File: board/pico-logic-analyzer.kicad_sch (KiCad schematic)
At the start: 25 parts, among them J1 Conn_02x03_Odd_Even, J11 Conn_01x01, SW1 SW_Push, U1 LM2665M6, U2 LM4040DBZ-5

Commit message: added export script
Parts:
- A1: footprint Module_RaspberryPi_Pico:RaspberryPi_Pico_Common_THT -> Module_RaspberryPi_Pico:RaspberryPi_Pico_Common
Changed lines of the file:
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@@
 		(at 128.27 194.31 0)
 		(unit 1)
-		(exclude_from_sim no)
+		(exclude_from_sim yes)
 		(in_bom no)
 		(on_board no)
@@
 			)
 		)
-		(property "Sim.Enable" "0"
-			(at 128.27 194.31 0)
-			(effects
-				(font
-					(size 1.27 1.27)
-				)
-				(hide yes)
-			)
-		)
 		(instances
 			(project "pico-logic-analyzer"
@@
 		(at 110.49 195.58 0)
 		(unit 1)
-		(exclude_from_sim no)
+		(exclude_from_sim yes)
 		(in_bom no)
 		(on_board no)
@@
 		)
 		(property "Description" "Open Hardware logo, small"
-			(at 110.49 195.58 0)
-			(effects
-				(font
-					(size 1.27 1.27)
-				)
-				(hide yes)
-			)
-		)
-		(property "Sim.Enable" "0"
 			(at 110.49 195.58 0)
 			(effects
@@
 			)
 		)
-		(property "Footprint" "Module_RaspberryPi_Pico:RaspberryPi_Pico_Common_THT"
+		(property "Footprint" "Module_RaspberryPi_Pico:RaspberryPi_Pico_Common"
 			(at 148.59 139.7 0)
 			(effects

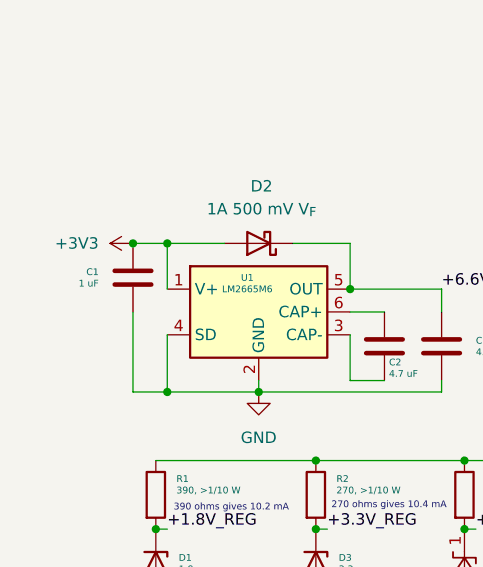
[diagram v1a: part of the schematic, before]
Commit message: 2.0 first commit * started switching caps to standard value of 0603 4.7uF (which is overkill everywhere) * tidied up some silkscreen * replaced 4x100kOhm pullup resistors with 1 array (of the same values) * made some space for the zener clamping circuit (will still be a very tight fit)
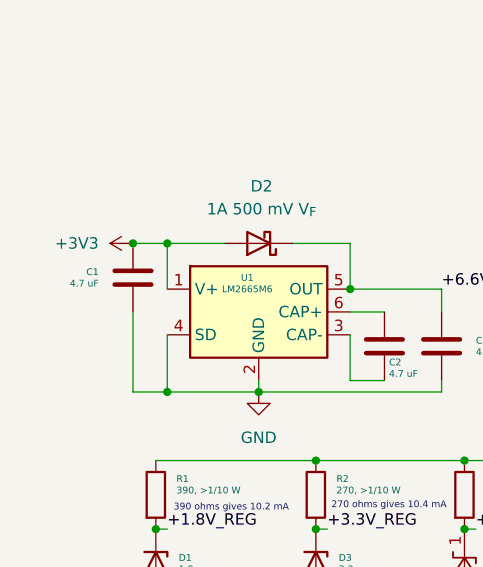
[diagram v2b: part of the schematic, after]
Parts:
- A1: footprint Module_RaspberryPi_Pico:RaspberryPi_Pico_Common -> Module_RaspberryPi_Pico:RaspberryPi_Pico_Common_THT
- C1: value 1 uF -> 4.7 uF; footprint Capacitor_SMD:C_0402_1005Metric -> Capacitor_SMD:C_0603_1608Metric
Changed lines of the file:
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@@
 			)
 		)
-		(property "Value" "1 uF"
+		(property "Value" "4.7 uF"
 			(at 29.21 139.0649 0)
 			(effects
@@
 			)
 		)
-		(property "Footprint" "Capacitor_SMD:C_0402_1005Metric"
+		(property "Footprint" "Capacitor_SMD:C_0603_1608Metric"
 			(at 33.9852 134.62 0)
 			(effects
@@
 			)
 		)
-		(property "Footprint" "Module_RaspberryPi_Pico:RaspberryPi_Pico_Common"
+		(property "Footprint" "Module_RaspberryPi_Pico:RaspberryPi_Pico_Common_THT"
 			(at 148.59 139.7 0)
 			(effects

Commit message: remove 3.3v zener from sch - start to switch to stdlib rpi pico -
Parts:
- removed D3: 3.3v, Diode_SMD:D_SOD-123, symbol Device:D_Zener
- removed R2: 270, >1/10 W, Resistor_SMD:R_0402_1005Metric, symbol Device:R
- removed TP1, TP2, TP3: TestPoint, TestPoint:TestPoint_Pad_D1.0mm, symbol Connector:TestPoint
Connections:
- net +3.3V_REG: no longer names the net of A1.35 (ADC_VREF)
- no-connect marks 8 -> 9
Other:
- note removed: "270 ohms gives 10.4 mA"

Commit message: layout overhaul backside pico now, which significantly reduces the size of the board and lets me do less suspect routing need to finish power delivery network for 3.3v, 5v reference, and 1.8v reference rails
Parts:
- removed A1: RaspberryPi_Pico, Module_RaspberryPi_Pico:RaspberryPi_Pico_Common_THT, symbol MCU_Module_RaspberryPi_Pico:RaspberryPi_Pico
- removed H2, H3: MountingHole, MountingHole:MountingHole_3.2mm_M3, symbol Mechanical:MountingHole
- removed H6: MountingHole, Symbol:KiCad-Logo2_5mm_SilkScreen, symbol Graphic:SYM_Arrow_Tiny
- added A2: RaspberryPi_Pico, asa-lib:RaspberryPi_Pico_SMD, symbol MCU_Module:RaspberryPi_Pico_Debug
- G1: renamed from H5; value MountingHole -> oshw!
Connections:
- net +3V3: now also A2.36 (3V3)
- net GND: now also A2.13 (GND), A2.18 (GND), A2.23 (GND), A2.28 (GND), A2.3 (GND), A2.33 (AGND), A2.38 (GND), A2.8 (GND), A2.D2 (GND)
- net at SW1.1: now also A2.30 (RUN)
- net A0_IN renamed A0
- net A0: now also A2.31 (GPIO26_ADC0)
- net A1_IN renamed A1
- net A1: now also A2.32 (GPIO27_ADC1)
- net A2_IN renamed A2
- net A2: now also A2.34 (GPIO28_ADC2)
- new net IO02: A2.4 (GPIO2)
- new net IO03: A2.5 (GPIO3)
- new net IO04: A2.6 (GPIO4)
- new net IO05: A2.7 (GPIO5)
- new net IO12: A2.16 (GPIO12)
- new net IO13: A2.17 (GPIO13)
- new net IO14: A2.19 (GPIO14)
- new net IO15: A2.20 (GPIO15)
- new net IO16: A2.21 (GPIO16)
- new net IO17: A2.22 (GPIO17)
- new net IO18: A2.24 (GPIO18)
- new net IO19: A2.25 (GPIO19)
- no-connect marks 9 -> 14
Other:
- removed sheet Analog Divider Selector 0
- removed sheet Analog Divider Selector 1
- removed sheet Analog Divider Selector 2
- moved on the sheet: G1, SW1

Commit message: backup commit before project structure overhaul
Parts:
- TP1: renamed from TP4; footprint TestPoint:TestPoint_Pad_D1.0mm -> TestPoint:TestPoint_Pad_D1.5mm; now left out of the parts list
- renumbered A2 to A1, C2 to C3, C1 to C4, C3 to C5, D2 to D3, D1 to D4, H4 to H2, J1 to J2, J11 to J8, R3 to R2, SW1 to SW2, U1 to U3
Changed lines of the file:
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@@
 		(on_board yes)
 		(dnp no)
-		(property "Reference" "R3"
+		(property "Reference" "R2"
 			(at 72.136 160.782 0)
 			(effects
@@
 			(project ""
 				(path "/7cf22b58-3beb-442b-8c1f-74d205325af0"
-					(reference "R3")
+					(reference "R2")
 					(unit 1)
 				)
@@
 		(dnp no)
 		(fields_autoplaced yes)
-		(property "Reference" "A2"
+		(property "Reference" "A1"
 			(at 140.6241 133.35 0)
 			(effects
@@
 			(project ""
 				(path "/7cf22b58-3beb-442b-8c1f-74d205325af0"
-					(reference "A2")
+					(reference "A1")
 					(unit 1)
 				)
@@
 		(on_board yes)
 		(dnp no)
-		(property "Reference" "C2"
+		(property "Reference" "C3"
 			(at 61.468 147.828 0)
 			(effects
@@
 			(project ""
 				(path "/7cf22b58-3beb-442b-8c1f-74d205325af0"
-					(reference "C2")
+					(reference "C3")
 					(unit 1)
 				)
@@
 		(on_board yes)
 		(dnp no)
-		(property "Reference" "C1"
+		(property "Reference" "C4"
 			(at 29.21 137.7949 0)
 			(effects
@@
 			(project "pico-logic-analyzer"
 				(path "/7cf22b58-3beb-442b-8c1f-74d205325af0"
-					(reference "C1")
+					(reference "C4")
 					(unit 1)
 				)
@@
 		(dnp no)
 		(fields_autoplaced yes)
-		(property "Reference" "J1"
+		(property "Reference" "J2"
 			(at 264.16 100.33 0)
 			(effects
@@
 			(project ""
 				(path "/7cf22b58-3beb-442b-8c1f-74d205325af0"
-					(reference "J1")
+					(reference "J2")
 					(unit 1)
 				)
@@
 		(on_board yes)
 		(dnp no)
-		(property "Reference" "SW1"
+		(property "Reference" "SW2"
 			(at 110.49 73.66 0)
 			(effects
@@
 			(project ""
 				(path "/7cf22b58-3beb-442b-8c1f-74d205325af0"
-					(reference "SW1")
+					(reference "SW2")
 					(unit 1)
 				)
@@
 		(dnp no)
 		(fields_autoplaced yes)
-		(property "Reference" "D1"
+		(property "Reference" "D4"
 			(at 38.1 169.5449 90)
 			(effects
@@
 			(project ""
 				(path "/7cf22b58-3beb-442b-8c1f-74d205325af0"
-					(reference "D1")
+					(reference "D4")
 					(unit 1)
 				)
@@
 		(dnp no)
 		(fields_autoplaced yes)
-		(property "Reference" "C3"
+		(property "Reference" "C5"
 			(at 71.12 145.4149 0)
 			(effects
@@
 			(project "pico-logic-analyzer"
 				(path "/7cf22b58-3beb-442b-8c1f-74d205325af0"
-					(reference "C3")
+					(reference "C5")
 					(unit 1)
 				)
@@
 		(unit 1)
 		(exclude_from_sim no)
-		(in_bom yes)
+		(in_bom no)
 		(on_board yes)
 		(dnp no)
 		(fields_autoplaced yes)
-		(property "Reference" "TP4"
+		(property "Reference" "TP1"
 			(at 130.81 175.1329 0)
 			(effects
@@
 			)
 		)
-		(property "Footprint" "TestPoint:TestPoint_Pad_D1.0mm"
+		(property "Footprint" "TestPoint:TestPoint_Pad_D1.5mm"
 			(at 133.35 179.07 0)
 			(effects
@@
 			)
 		)
-		(property "Description" "test point"
+		(property "Description" ""
 			(at 128.27 179.07 0)
 			(effects
@@
 			(project "pico-logic-analyzer"
 				(path "/7cf22b58-3beb-442b-8c1f-74d205325af0"
-					(reference "TP4")
+					(reference "TP1")
 					(unit 1)
 				)
@@
 		(on_board yes)
 		(dnp no)
-		(property "Reference" "U1"
+		(property "Reference" "U3"
 			(at 45.72 138.43 0)
 			(effects
@@
 			(project ""
 				(path "/7cf22b58-3beb-442b-8c1f-74d205325af0"
-					(reference "U1")
+					(reference "U3")
 					(unit 1)
 				)
@@
 		(dnp no)
 		(fields_autoplaced yes)
-		(property "Reference" "J11"
+		(property "Reference" "J8"
 			(at 121.92 157.4799 0)
 			(effects
@@
 			(project ""
 				(path "/7cf22b58-3beb-442b-8c1f-74d205325af0"
-					(reference "J11")
+					(reference "J8")
 					(unit 1)
 				)
@@
 		(on_board yes)
 		(dnp no)
-		(property "Reference" "H4"
+		(property "Reference" "H2"
 			(at 234.696 36.83 0)
 			(effects
@@
 			(project "pico-logic-analyzer"
 				(path "/7cf22b58-3beb-442b-8c1f-74d205325af0"
-					(reference "H4")
+					(reference "H2")
 					(unit 1)
 				)
@@
 		(dnp no)
 		(fields_autoplaced yes)
-		(property "Reference" "D2"
+		(property "Reference" "D3"
 			(at 47.3075 128.27 0)
 			(effects
@@
 			(project ""
 				(path "/7cf22b58-3beb-442b-8c1f-74d205325af0"
-					(reference "D2")
-					(unit 1)
-				)
+					(reference "D3")
+					(unit 1)
+				)
